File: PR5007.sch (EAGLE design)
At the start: 38 parts

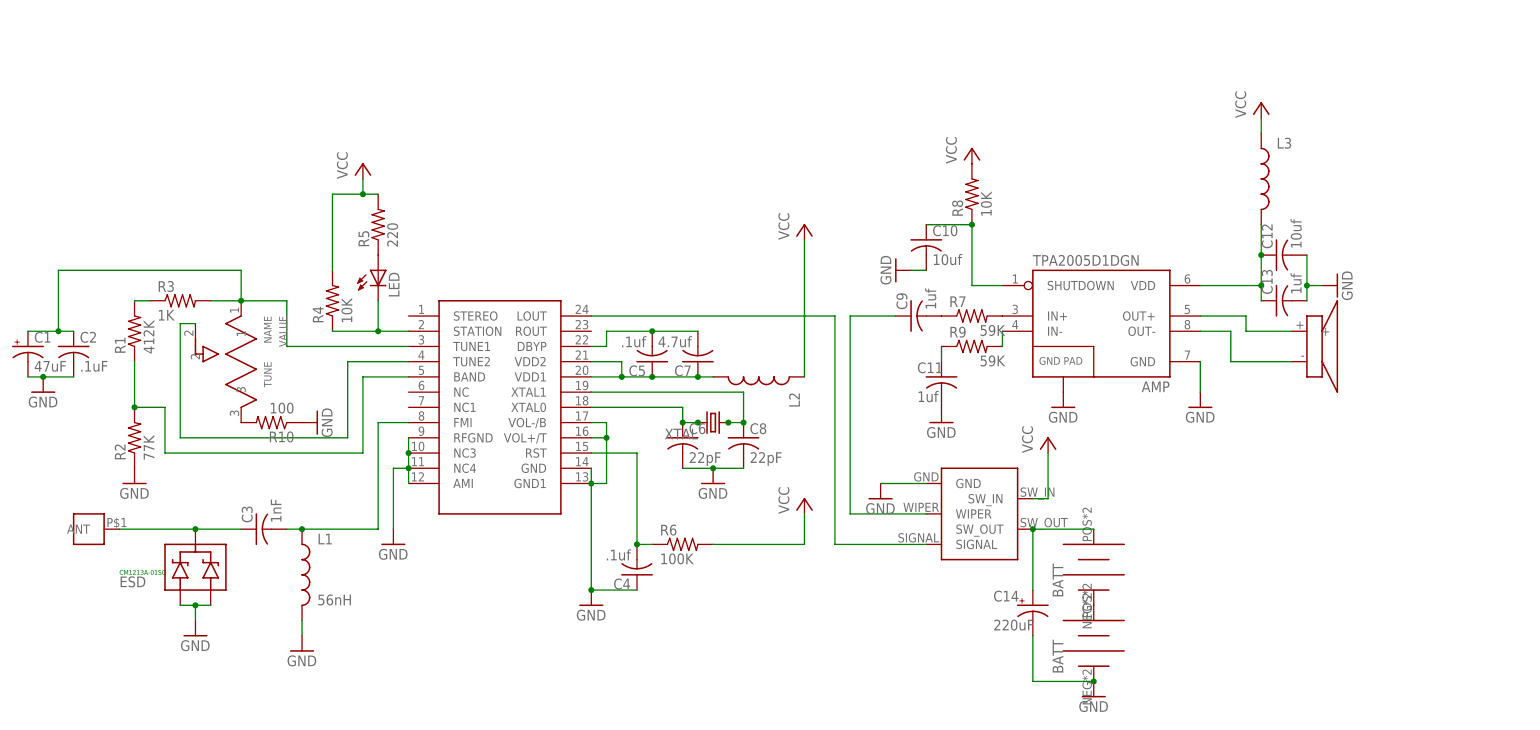
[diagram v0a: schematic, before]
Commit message: New Board Layout
Made some of the edits based on the workflowy feature request list.
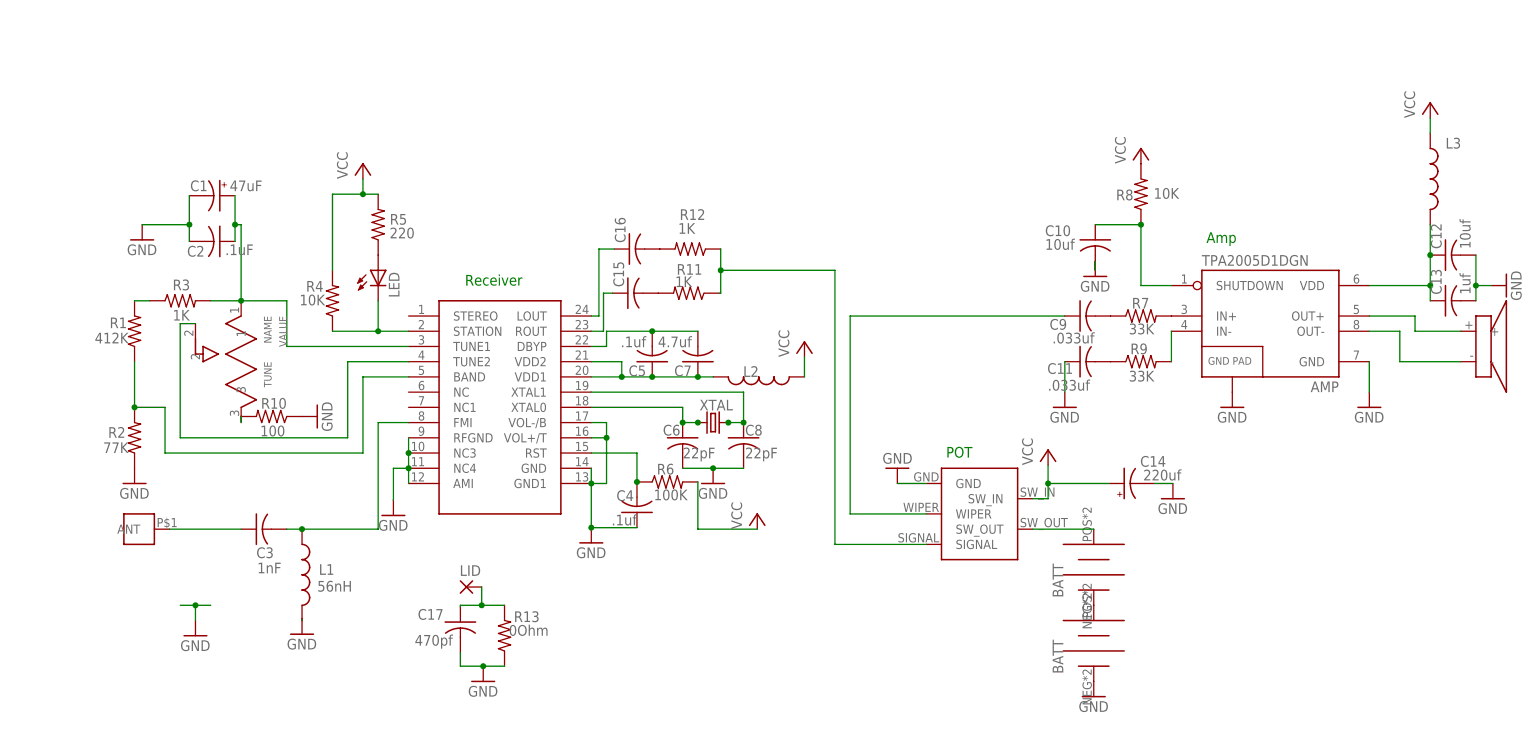
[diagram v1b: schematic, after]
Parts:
- removed ESD: CM1213A-01SO, SparkFun-DiscreteSemi:MMBZ27VCLT1
- added C15, C16: (no value), resistor:C-USC0805
- added C17: 470pf, resistor:C-USC0805
- added LID: (no value), wirepad:2,54/1,0
- added R11, R12: 1K, resistor:R-US_R0603
- added R13: 0Ohm, resistor:R-US_R0603
- C11, C9: value 1uf -> .033uf
- C14: value 220uF -> 220uf; device resistor-copy:CPOL-USE2.5-5 -> CPOL-US-LongPads :CPOL-USE2-5
- R7, R9: value 59K -> 33K
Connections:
- new net N$21: C15.2, R11.2
- new net N$30: C16.2, R12.2
- new net N$31: C15.1, SI4831.ROUT
- new net N$33: C16.1, SI4831.LOUT
- new net N$34: C17.1, LID.P, R13.2
- net GND: now also C11.1, C17.2, R13.1; no longer C11.2, ESD.A1, ESD.A2
- net N$19: no longer ESD.C
- net N$3: now also C11.2; no longer C11.1
- net N$32: no longer C14.+
- net N$5: now also R11.1, R12.1; no longer SI4831.LOUT
- net VCC: now also C14.+
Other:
- note added: "Amp"
- note added: "POT"
- note added: "Receiver"
- note removed: "CM1213A-01SO"
- moved on the sheet: AMP, C1, C10, C11, C12, C13, C14, C2, C4, C9, L3, R10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

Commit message: Updated 5007
Update from 5.14. speaker wires no longer crossing
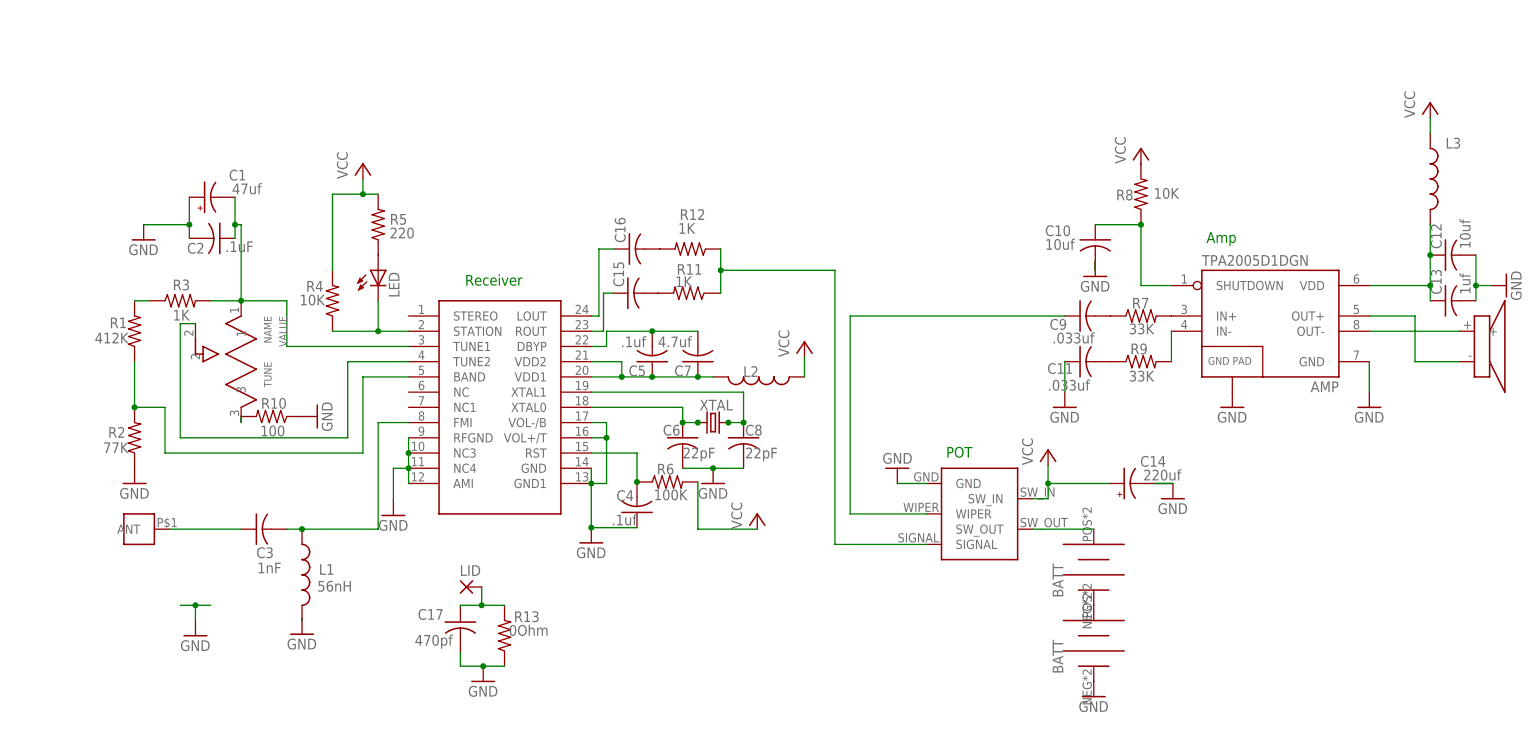
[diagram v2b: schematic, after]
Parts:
- C1: value 47uF -> 47uf; device resistor-copy:CPOL-USE2-5 -> CPOL-US-LongPads :CPOL-USE2-5
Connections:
- net GND: now also C1.+; no longer C1.-
- net N$22: now also C1.-; no longer C1.+
- net N$23: now also U$3.-; no longer U$3.+
- net N$24: now also U$3.+; no longer U$3.-
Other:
- moved on the sheet: C1, C2
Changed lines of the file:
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@@
 <part name="R3" library="resistor" deviceset="R-US_" device="R0603" value="1K"/>
 <part name="R1" library="resistor" deviceset="R-US_" device="R0603" value="412K"/>
-<part name="C1" library="resistor-copy" deviceset="CPOL-US" device="E2-5" value="47uF"/>
 <part name="C2" library="resistor" deviceset="C-US" device="C0603" value=".1uF"/>
 <part name="GND13" library="SparkFun-Aesthetics" deviceset="GND" device=""/>
@@
 <part name="LID" library="wirepad" deviceset="2,54/1,0" device=""/>
 <part name="C14" library="CPOL-US-LongPads " deviceset="CPOL-US" device="E2-5" value="220uf"/>
+<part name="C1" library="CPOL-US-LongPads " deviceset="CPOL-US" device="E2-5" value="47uf"/>
 </parts>
 <sheets>
@@
 <attribute name="VALUE" x="-23.876" y="83.566" size="1.778" layer="96" rot="R180"/>
 </instance>
-<instance part="C1" gate="G$1" x="-8.636" y="106.426" smashed="yes" rot="R270">
-<attribute name="NAME" x="-13.589" y="107.188" size="1.778" layer="95"/>
-<attribute name="VALUE" x="-6.985" y="107.188" size="1.778" layer="96"/>
-</instance>
-<instance part="C2" gate="G$1" x="-8.636" y="98.806" smashed="yes" rot="R270">
-<attribute name="NAME" x="-14.097" y="96.266" size="1.778" layer="95"/>
-<attribute name="VALUE" x="-7.747" y="96.52" size="1.778" layer="96"/>
-</instance>
-<instance part="GND13" gate="1" x="-21.59" y="99.06"/>
+<instance part="C2" gate="G$1" x="-8.636" y="99.314" smashed="yes" rot="R270">
+<attribute name="NAME" x="-14.097" y="96.774" size="1.778" layer="95"/>
+<attribute name="VALUE" x="-7.747" y="97.028" size="1.778" layer="96"/>
+</instance>
+<instance part="GND13" gate="1" x="-21.336" y="99.06"/>
 <instance part="GND14" gate="1" x="137.16" y="22.86"/>
 <instance part="P+6" gate="VCC" x="129.54" y="64.008"/>
-<instance part="U$3" gate="G$1" x="200.914" y="81.28"/>
+<instance part="U$3" gate="G$1" x="200.66" y="81.28"/>
 <instance part="ANT" gate="G$1" x="-22.098" y="50.8" smashed="yes" rot="R90"/>
 <instance part="U$5" gate="G$1" x="116.84" y="53.34"/>
@@
 <attribute name="NAME" x="149.225" y="62.992" size="1.778" layer="95" rot="R180"/>
 <attribute name="VALUE" x="151.765" y="60.706" size="1.778" layer="96" rot="R180"/>
+</instance>
+<instance part="C1" gate="G$1" x="-11.176" y="106.172" smashed="yes" rot="R90">
+<attribute name="NAME" x="-4.191" y="110.744" size="1.778" layer="95" rot="R180"/>
+<attribute name="VALUE" x="-1.651" y="108.458" size="1.778" layer="96" rot="R180"/>
 </instance>
 </instances>
@@
 </segment>
 <segment>
-<pinref part="C1" gate="G$1" pin="-"/>
 <pinref part="C2" gate="G$1" pin="2"/>
-<wire x1="-13.716" y1="106.426" x2="-13.716" y2="101.6" width="0.1524" layer="91"/>
+<wire x1="-13.716" y1="106.172" x2="-13.716" y2="101.6" width="0.1524" layer="91"/>
 <pinref part="GND13" gate="1" pin="GND"/>
-<wire x1="-13.716" y1="101.6" x2="-13.716" y2="98.806" width="0.1524" layer="91"/>
-<wire x1="-21.59" y1="101.6" x2="-13.716" y2="101.6" width="0.1524" layer="91"/>
+<wire x1="-13.716" y1="101.6" x2="-13.716" y2="99.314" width="0.1524" layer="91"/>
+<wire x1="-21.336" y1="101.6" x2="-13.716" y2="101.6" width="0.1524" layer="91"/>
 <junction x="-13.716" y="101.6"/>
+<pinref part="C1" gate="G$1" pin="+"/>
 </segment>
 <segment>
@@
 <wire x1="147.32" y1="58.42" x2="150.368" y2="58.42" width="0.1524" layer="91"/>
 <pinref part="C14" gate="G$1" pin="-"/>
+<wire x1="147.32" y1="58.42" x2="150.368" y2="58.42" width="0.1524" layer="91"/>
 </segment>
 <segment>
@@
 </segment>
 </net>
-<net name="N$24" class="0">
-<segment>
-<pinref part="U$3" gate="G$1" pin="-"/>
-<wire x1="198.374" y1="78.74" x2="188.214" y2="78.74" width="0.1524" layer="91"/>
-<pinref part="AMP" gate="G$1" pin="OUT-"/>
-<wire x1="183.134" y1="83.82" x2="188.214" y2="83.82" width="0.1524" layer="91"/>
-<wire x1="188.214" y1="83.82" x2="188.214" y2="78.74" width="0.1524" layer="91"/>
-</segment>
-</net>
 <net name="N$29" class="0">
 <segment>
@@
 <net name="N$23" class="0">
 <segment>
-<pinref part="U$3" gate="G$1" pin="+"/>
-<wire x1="198.374" y1="83.82" x2="190.754" y2="83.82" width="0.1524" layer="91"/>
-<wire x1="190.754" y1="83.82" x2="190.754" y2="86.36" width="0.1524" layer="91"/>
 <pinref part="AMP" gate="G$1" pin="OUT+"/>
 <wire x1="190.754" y1="86.36" x2="183.134" y2="86.36" width="0.1524" layer="91"/>
+<wire x1="190.754" y1="86.36" x2="190.754" y2="78.74" width="0.1524" layer="91"/>
+<pinref part="U$3" gate="G$1" pin="-"/>
+<wire x1="190.754" y1="78.74" x2="198.12" y2="78.74" width="0.1524" layer="91"/>
 </segment>
 </net>
@@
 <segment>
 <pinref part="C2" gate="G$1" pin="1"/>
-<pinref part="C1" gate="G$1" pin="+"/>
-<wire x1="-6.096" y1="106.426" x2="-6.096" y2="101.6" width="0.1524" layer="91"/>
+<wire x1="-6.096" y1="106.172" x2="-6.096" y2="101.6" width="0.1524" layer="91"/>
 <pinref part="SI4831" gate="G$1" pin="TUNE1"/>
-<wire x1="-6.096" y1="101.6" x2="-6.096" y2="98.806" width="0.1524" layer="91"/>
+<wire x1="-6.096" y1="101.6" x2="-6.096" y2="99.314" width="0.1524" layer="91"/>
 <wire x1="22.86" y1="81.28" x2="2.54" y2="81.28" width="0.1524" layer="91"/>
 <wire x1="2.54" y1="81.28" x2="2.54" y2="88.9" width="0.1524" layer="91"/>
@@
 <wire x1="-5.08" y1="101.6" x2="-5.08" y2="88.9" width="0.1524" layer="91"/>
 <junction x="-6.096" y="101.6"/>
+<pinref part="C1" gate="G$1" pin="-"/>
 </segment>
 </net>
@@
 </segment>
 </net>
+<net name="N$24" class="0">
+<segment>
+<pinref part="AMP" gate="G$1" pin="OUT-"/>
+<pinref part="U$3" gate="G$1" pin="+"/>
+<wire x1="183.134" y1="83.82" x2="198.12" y2="83.82" width="0.1524" layer="91"/>
+</segment>
+</net>

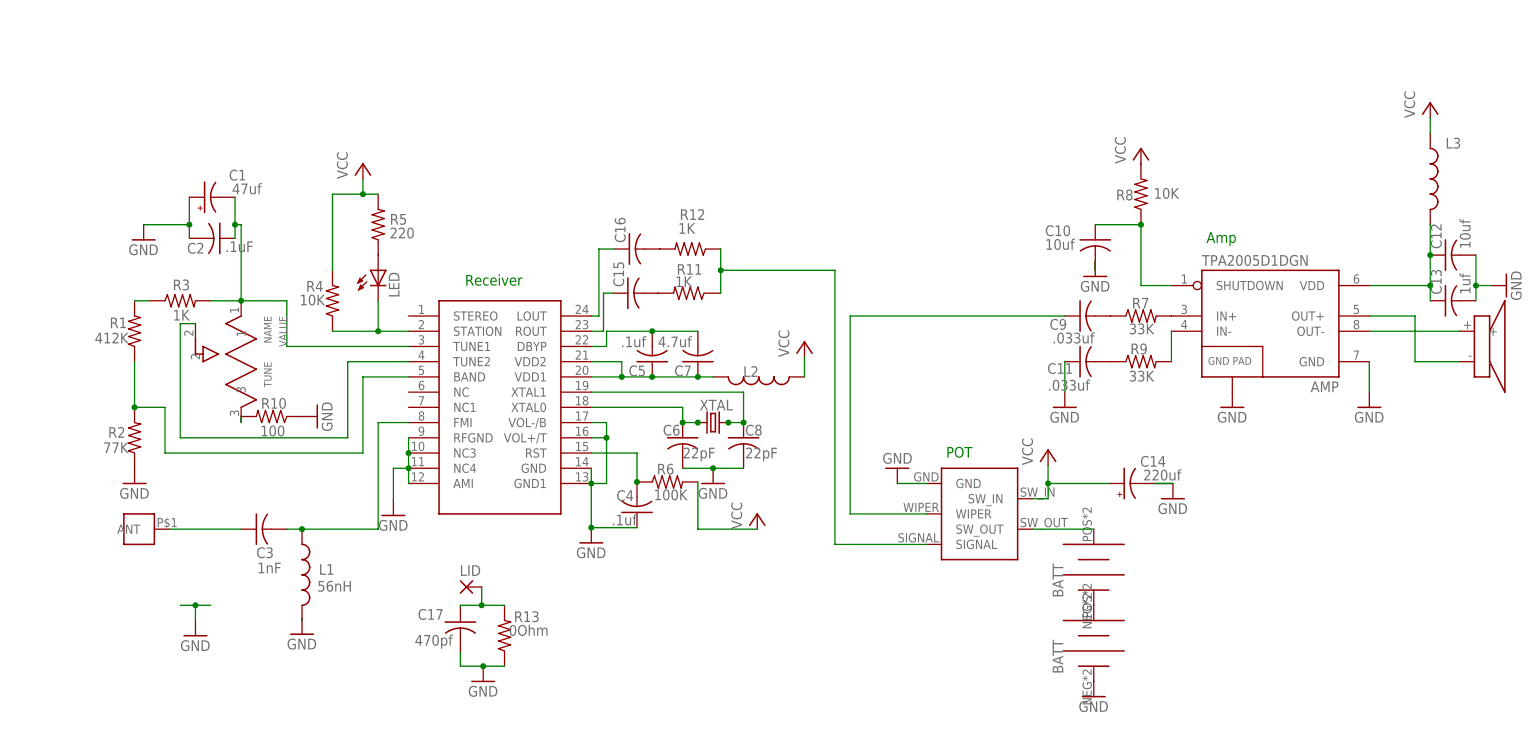
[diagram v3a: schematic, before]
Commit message: Updates Post-Phone Call
Added C18,C19,C20 in parallel with existing decoupling caps.
Reworked routing around FM IC and Amp
Added coupling caps and resistors for L+R out.
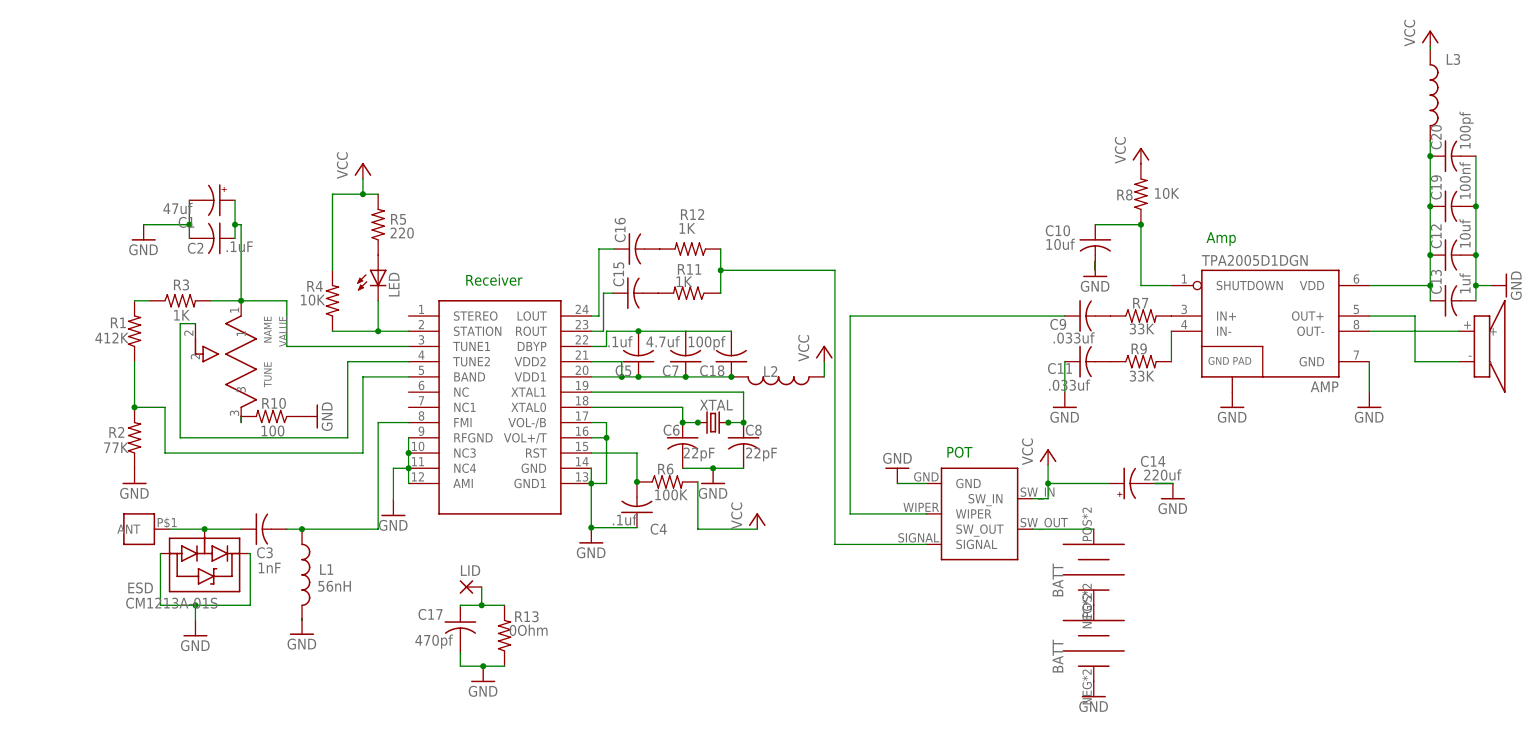
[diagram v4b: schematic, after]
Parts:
- added C18, C20: 100pf, resistor:C-USC0603
- added C19: 100nf, resistor:C-USC0603
- added ESD: CM1213A-01S, PubRadioLib:CM1213A-01S
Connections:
- net GND: now also C1.-, C19.2, C20.2, ESD.VN, ESD.VP; no longer C1.+
- net N$16: now also C18.1
- net N$17: now also C19.1, C20.1
- net N$19: now also ESD.CH
- net N$22: now also C1.+; no longer C1.-
- net N$6: now also C18.2
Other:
- moved on the sheet: C1, C5, C7, L2, L3
